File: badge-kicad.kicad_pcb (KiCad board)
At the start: 2 copper layers, 152.7 x 76.7 mm, 124 parts, among them J2 JTAG, P2 CONN_02X20, P3 FTDI BACKUP, P4 USB_MICRO_RIGHT, P5 LED OUT (DNP), SW1 RESET, SW2 POWERON, SW3 TM1000, SW4 UP, SW5 DN, SW6 LEFT, SW7 RIGHT, SW8 ENTER, U1 WS2812B, U10 WS2812B, U11 WS2812B, U12 WS2812B, U13 MKW01Z128, U14 FT232RL SSOP, U15 MF-REG-SOT235-3.3V-300mA, U16 MCP73831T-2ACI/OT, U18 LM386, U2 WS2812B, U3 WS2812B, U4 WS2812B, U5 WS2812B, U6 WS2812B, U7 WS2812B, U8 WS2812B, U9 WS2812B, Y1 EXS00A-CS02368

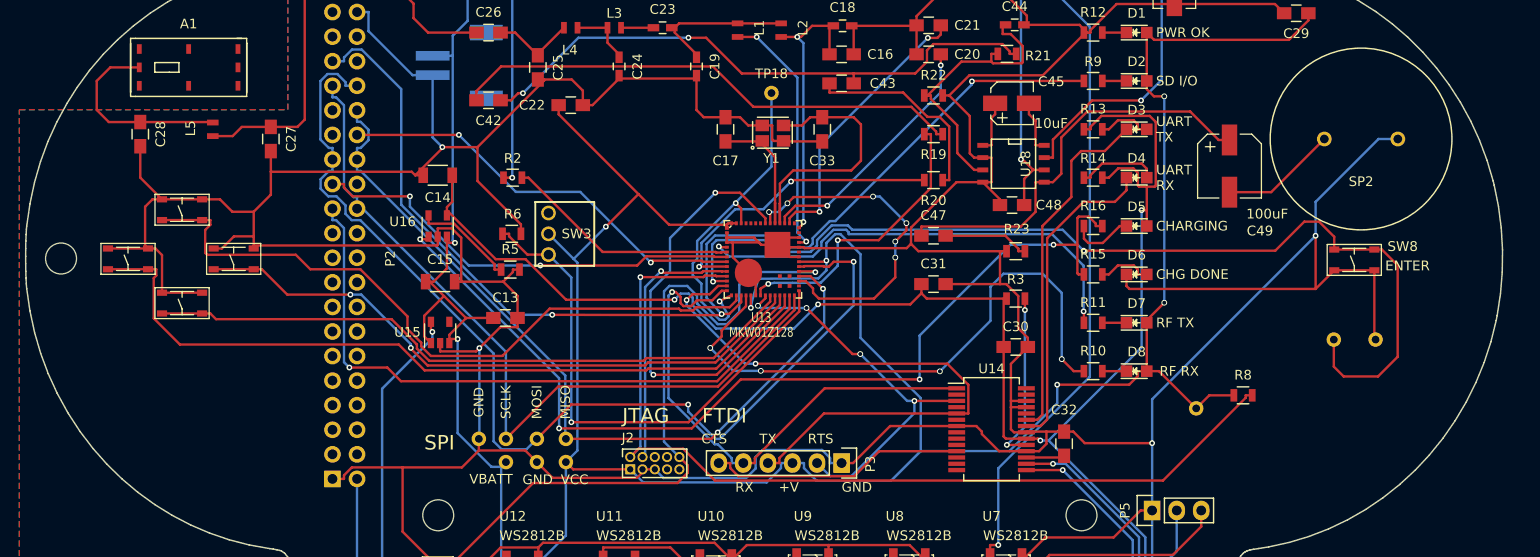
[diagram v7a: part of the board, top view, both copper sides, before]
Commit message: add laurel designs back, switch some caps to 0603 based on BOM
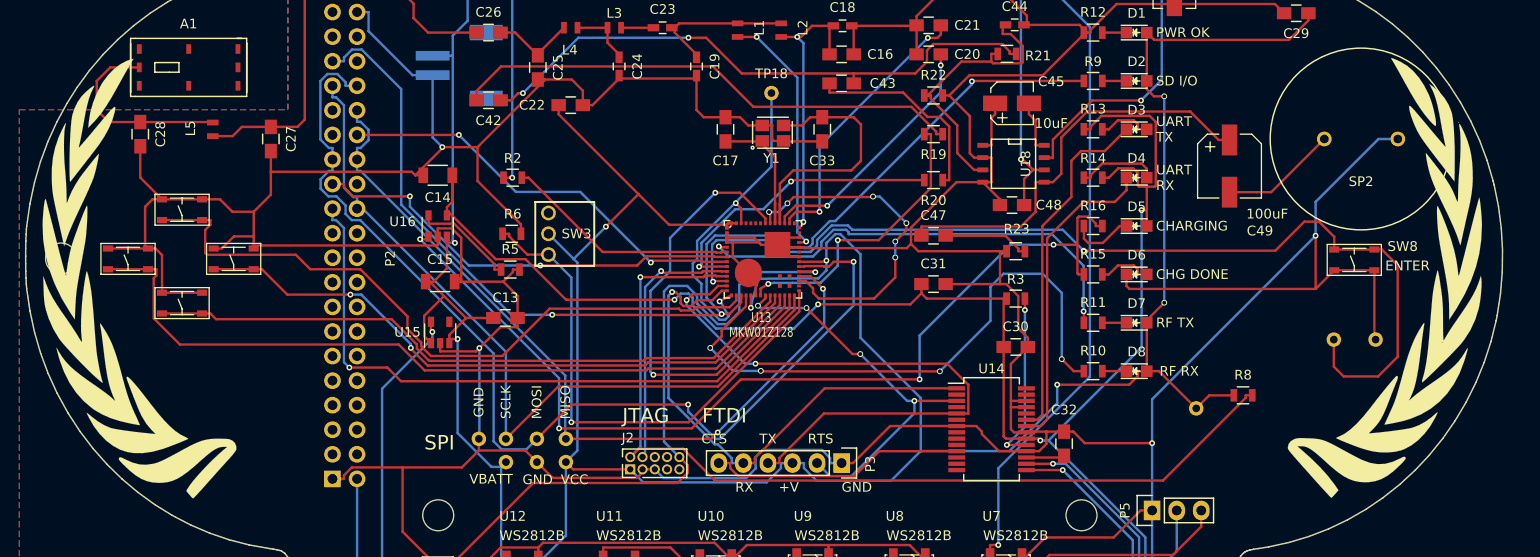
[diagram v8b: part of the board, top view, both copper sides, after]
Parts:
- added ?: , logos:laurel, F.Cu at (82.4, 91.1)
- added ?: , logos:laurel_right, F.Cu at (215.2, 91.0)
